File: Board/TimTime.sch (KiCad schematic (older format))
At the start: 56 parts, among them IC2 MCP73834-CNI_MF, J7 Conn_01x02, U1 STM32L433CCTx, Y1 7P-19.200MBP-T

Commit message: Initial Board Layout
Rough pass of component layout. Working down the overall footprint of the device. Also updated a couple components in the schematic.
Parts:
- removed SW? (x3): SW_Push, symbol Switch:SW_Push
- added J6: Conn_01x02, Connector_PinHeader_2.54mm:PinHeader_1x02_P2.54mm_Vertical, symbol Connector_Generic:Conn_01x02
- added S1, S2: PTS647SM70SMTR2LFS, PTS647SM70SMTR2LFS:PTS647SM38SMTR2LFS, symbol PTS647SM70SMTR2LFS:PTS647SM70SMTR2LFS
- added S3: KSS241GLFS, KSS241GLFS:KSS241GLFS, symbol KSS241GLFS:KSS241GLFS
- Brd1: renamed from Brd?; footprint (none) -> SSD1306:128x64OLED
- C13: renamed from C12; value 4.7uF -> 12uF
- D2: renamed from D?; footprint (none) -> Diode_SMD:D_SOD-123
- IC2: renamed from IC?; footprint SOT95P280X100-5N -> LT1761ES5-2:SOT95P280X100-5N
- J1: renamed from J?; footprint GCT_USB4085-GF-A_REVA -> USB4085-GF-A_REVA:GCT_USB4085-GF-A_REVA
- J2: renamed from J?; footprint CUI_SJ1-3523NG -> SJ1-3523NG:CUI_SJ1-3523NG
- J3: renamed from J?; footprint (none) -> Connector_PinHeader_2.54mm:PinHeader_1x04_P2.54mm_Vertical
- J4: renamed from J?; footprint (none) -> Connector_PinHeader_2.54mm:PinHeader_1x06_P2.54mm_Vertical
- R10, R11, R9: renamed from R?; footprint (none) -> Resistor_SMD:R_0603_1608Metric_Pad1.05x0.95mm_HandSolder
- U2: renamed from U?; footprint SOT95P280X145-5N -> 24AA00T_OT:SOT95P280X145-5N
- gave numbers to parts that had none: 8
- renumbered C13 to C12, C11 to C15, C14 to C16, C3 to C4, C4 to C5, C5 to C6, IC2 to IC1, J7 to J5, R5 to R1, R9 to R12, R10 to R13, R11 to R16, R12 to R17, R13 to R18, R6 to R2, R1 to R4, R2 to R5, R3 to R6, R4 to R8
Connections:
- net labels added: OSC
- wire segments 199 -> 228
- no-connect marks 22 -> 20
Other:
- note added: "OSC"
- moved on the sheet: J4, J5, R15, R19

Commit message: Update layout
Smaller footprint
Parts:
- added R20: 2K, Resistor_SMD:R_0603_1608Metric_Pad1.05x0.95mm_HandSolder, symbol Device:R_Small
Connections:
- net GND: now also R20.2; no longer R16.2
- new net: R16.2, R20.1
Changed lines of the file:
@@
 L power:GND #PWR043
 U 1 1 5FE4CC6E
-P 10000 3700
-F 0 "#PWR043" H 10000 3450 50  0001 C CNN
-F 1 "GND" H 10000 3550 50  0000 C CNN
-F 2 "" H 10000 3700 50  0001 C CNN
-F 3 "" H 10000 3700 50  0001 C CNN
-	1    10000 3700
+P 10000 3950
+F 0 "#PWR043" H 10000 3700 50  0001 C CNN
+F 1 "GND" H 10000 3800 50  0000 C CNN
+F 2 "" H 10000 3950 50  0001 C CNN
+F 3 "" H 10000 3950 50  0001 C CNN
+	1    10000 3950
 	1    0    0    -1
 $EndComp
@@
 Wire Wire Line
 	10900 5900 10900 6000
+$Comp
+L Device:R_Small R20
+U 1 1 60DAE3C0
+P 10000 3800
+F 0 "R20" H 10059 3846 50  0000 L CNN
+F 1 "2K" H 10059 3755 50  0000 L CNN
+F 2 "Resistor_SMD:R_0603_1608Metric_Pad1.05x0.95mm_HandSolder" H 10000 3800 50  0001 C CNN
+F 3 "~" H 10000 3800 50  0001 C CNN
+	1    10000 3800
+	1    0    0    -1
+$EndComp
+Wire Wire Line
+	10000 3900 10000 3950
 $EndSCHEMATC

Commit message: Updated routing
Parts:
- removed C2: 12uF, Capacitor_SMD:C_0603_1608Metric_Pad1.05x0.95mm_HandSolder, symbol Device:C_Small
- removed R4: 1M, Resistor_SMD:R_0603_1608Metric_Pad1.05x0.95mm_HandSolder, symbol Device:R_Small
- Brd1: symbol SSD1306-128x64_OLED:SSD1306 -> TimTime-rescue:SSD1306-SSD1306-128x64_OLED
- IC2: symbol LT1761ES5-2.8#TRMPBF:LT1761ES5-2.8#TRMPBF -> TimTime-rescue:LT1761ES5-2.8#TRMPBF-LT1761ES5-2.8#TRMPBF
- J1: symbol USB4085-GF-A_REVA:USB4085-GF-A_REVA -> TimTime-rescue:USB4085-GF-A_REVA-USB4085-GF-A_REVA
- J2: symbol SJ1-3523NG:SJ1-3523NG -> TimTime-rescue:SJ1-3523NG-SJ1-3523NG
- S1, S2: symbol PTS647SM70SMTR2LFS:PTS647SM70SMTR2LFS -> TimTime-rescue:PTS647SM70SMTR2LFS-PTS647SM70SMTR2LFS
- S3: symbol KSS241GLFS:KSS241GLFS -> TimTime-rescue:KSS241GLFS-KSS241GLFS
- U2: symbol 24AA00T_OT:24AA00T_OT -> TimTime-rescue:24AA00T_OT-24AA00T_OT
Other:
- note removed: "BOOT0 Reset"
- moved on the sheet: D1, R8
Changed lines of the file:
@@
 Text Notes 5950 1550 0    50   ~ 0
 MCU Analog Filter
-Text Notes 2400 3050 0    50   ~ 0
+Text Notes 1200 3050 0    50   ~ 0
 Status LED
 Wire Notes Line
-	1750 3100 1750 2000
-Wire Notes Line
-	2900 3100 1750 3100
-Wire Notes Line
-	2900 2000 2900 3100
-Wire Notes Line
-	1750 2000 2900 2000
-Wire Wire Line
-	2100 2750 2100 2850
+	550  3100 550  2000
+Wire Notes Line
+	1700 3100 550  3100
+Wire Notes Line
+	1700 2000 1700 3100
+Wire Notes Line
+	550  2000 1700 2000
+Wire Wire Line
+	900  2750 900  2850
 $Comp
 L power:GND #PWR011
 U 1 1 5FF4BF69
-P 2100 2850
-F 0 "#PWR011" H 2100 2600 50  0001 C CNN
-F 1 "GND" H 2105 2677 50  0000 C CNN
-F 2 "" H 2100 2850 50  0001 C CNN
-F 3 "" H 2100 2850 50  0001 C CNN
-	1    2100 2850
-	1    0    0    -1
-$EndComp
-Wire Wire Line
-	2100 2450 2100 2550
-Wire Wire Line
-	2100 2150 2100 2250
-Wire Wire Line
-	2250 2150 2100 2150
-Text GLabel 2250 2150 2    50   Input ~ 0
+P 900 2850
+F 0 "#PWR011" H 900 2600 50  0001 C CNN
+F 1 "GND" H 905 2677 50  0000 C CNN
+F 2 "" H 900 2850 50  0001 C CNN
+F 3 "" H 900 2850 50  0001 C CNN
+	1    900  2850
+	1    0    0    -1
+$EndComp
+Wire Wire Line
+	900  2450 900  2550
+Wire Wire Line
+	900  2150 900  2250
+Wire Wire Line
+	1050 2150 900  2150
+Text GLabel 1050 2150 2    50   Input ~ 0
 LED_STATUS
 $Comp
 L Device:R_Small R8
 U 1 1 5FF3E941
-P 2100 2650
-F 0 "R8" H 2159 2696 50  0000 L CNN
-F 1 "30" H 2159 2605 50  0000 L CNN
-F 2 "Resistor_SMD:R_0603_1608Metric_Pad1.05x0.95mm_HandSolder" H 2100 2650 50  0001 C CNN
-F 3 "~" H 2100 2650 50  0001 C CNN
-	1    2100 2650
+P 900 2650
+F 0 "R8" H 959 2696 50  0000 L CNN
+F 1 "30" H 959 2605 50  0000 L CNN
+F 2 "Resistor_SMD:R_0603_1608Metric_Pad1.05x0.95mm_HandSolder" H 900 2650 50  0001 C CNN
+F 3 "~" H 900 2650 50  0001 C CNN
+	1    900  2650
 	1    0    0    -1
 $EndComp
@@
 L Device:LED_Small D1
 U 1 1 5FF3CEBF
-P 2100 2350
-F 0 "D1" V 2146 2280 50  0000 R CNN
-F 1 "BLUE" V 2055 2280 50  0000 R CNN
-F 2 "LED_SMD:LED_1206_3216Metric_Pad1.42x1.75mm_HandSolder" V 2100 2350 50  0001 C CNN
-F 3 "~" V 2100 2350 50  0001 C CNN
-	1    2100 2350
+P 900 2350
+F 0 "D1" V 946 2280 50  0000 R CNN
+F 1 "BLUE" V 855 2280 50  0000 R CNN
+F 2 "LED_SMD:LED_1206_3216Metric_Pad1.42x1.75mm_HandSolder" V 900 2350 50  0001 C CNN
+F 3 "~" V 900 2350 50  0001 C CNN
+	1    900  2350
 	0    -1   -1   0
 $EndComp
-Text Notes 600  3050 0    50   ~ 0
-BOOT0 Reset
-Wire Notes Line
-	550  3100 550  2000
-Wire Notes Line
-	1650 3100 550  3100
-Wire Notes Line
-	1650 2000 1650 3100
-Wire Notes Line
-	550  2000 1650 2000
 Text Notes 600  1900 0    50   ~ 0
 TXCO
@@
 Wire Notes Line
 	3350 1950 550  1950
-Wire Wire Line
-	1250 2550 1250 2500
-Connection ~ 1250 2550
-Wire Wire Line
-	1100 2550 1250 2550
-Wire Wire Line
-	1100 2500 1100 2550
-Wire Wire Line
-	1250 2600 1250 2550
-$Comp
-L power:GND #PWR08
-U 1 1 5FE06E7D
-P 1250 2600
-F 0 "#PWR08" H 1250 2350 50  0001 C CNN
-F 1 "GND" H 1255 2427 50  0000 C CNN
-F 2 "" H 1250 2600 50  0001 C CNN
-F 3 "" H 1250 2600 50  0001 C CNN
-	1    1250 2600
-	1    0    0    -1
-$EndComp
-Wire Wire Line
-	1250 2250 1250 2300
-Connection ~ 1250 2250
-Wire Wire Line
-	1100 2250 1250 2250
-Wire Wire Line
-	1100 2300 1100 2250
-Wire Wire Line
-	1250 2150 1250 2250
-Wire Wire Line
-	1150 2150 1250 2150
-$Comp
-L Device:C_Small C2
-U 1 1 5FE049E6
-P 1250 2400
-F 0 "C2" H 1342 2446 50  0000 L CNN
-F 1 "12uF" H 1342 2355 50  0000 L CNN
-F 2 "Capacitor_SMD:C_0603_1608Metric_Pad1.05x0.95mm_HandSolder" H 1250 2400 50  0001 C CNN
-F 3 "~" H 1250 2400 50  0001 C CNN
-	1    1250 2400
-	1    0    0    -1
-$EndComp
-Text GLabel 1150 2150 0    50   Input ~ 0
-BOOT0
-$Comp
-L Device:R_Small R4
-U 1 1 5FDB4DA9
-P 1100 2400
-F 0 "R4" V 904 2400 50  0000 C CNN
-F 1 "1M" V 995 2400 50  0000 C CNN
-F 2 "Resistor_SMD:R_0603_1608Metric_Pad1.05x0.95mm_HandSolder" H 1100 2400 50  0001 C CNN
-F 3 "~" H 1100 2400 50  0001 C CNN
-	1    1100 2400
-	1    0    0    -1
-$EndComp
-$Comp
-L LT1761ES5-2.8#TRMPBF:LT1761ES5-2.8#TRMPBF IC2
+$Comp
+L TimTime-rescue:LT1761ES5-2.8#TRMPBF-LT1761ES5-2.8#TRMPBF IC2
 U 1 1 609D162F
 P 8800 1150
@@
 	550  3150 1650 3150
 $Comp
-L USB4085-GF-A_REVA:USB4085-GF-A_REVA J1
+L TimTime-rescue:USB4085-GF-A_REVA-USB4085-GF-A_REVA J1
 U 1 1 60EA7903
 P 1300 5600
@@
 	1900 7750 550  7750
 $Comp
-L SJ1-3523NG:SJ1-3523NG J2
+L TimTime-rescue:SJ1-3523NG-SJ1-3523NG J2
 U 1 1 608E50D0
 P 2500 7300
@@
 NoConn ~ 3100 7300
 $Comp
-L 24AA00T_OT:24AA00T_OT U2
+L TimTime-rescue:24AA00T_OT-24AA00T_OT U2
 U 1 1 609233E5
 P 7100 5850
@@
 TC Input/Output
 $Comp
-L SSD1306-128x64_OLED:SSD1306 Brd1
+L TimTime-rescue:SSD1306-SSD1306-128x64_OLED Brd1
 U 1 1 60FA55A1
 P 2500 5100
@@
 	1000 950  1450 950
 $Comp
-L PTS647SM70SMTR2LFS:PTS647SM70SMTR2LFS S1
+L TimTime-rescue:PTS647SM70SMTR2LFS-PTS647SM70SMTR2LFS S1
 U 1 1 609708D6
 P 8500 6300
@@
 Connection ~ 8350 5850
 $Comp
-L PTS647SM70SMTR2LFS:PTS647SM70SMTR2LFS S2
+L TimTime-rescue:PTS647SM70SMTR2LFS-PTS647SM70SMTR2LFS S2
 U 1 1 60A438F2
 P 9500 6300
@@
 Connection ~ 9750 5900
 $Comp
-L KSS241GLFS:KSS241GLFS S3
+L TimTime-rescue:KSS241GLFS-KSS241GLFS S3
 U 1 1 60B48A83
 P 10600 5700

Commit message: V02 routing. VddUSB
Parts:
- added C17, C2: 1.2uF, Capacitor_SMD:C_0603_1608Metric_Pad1.08x0.95mm_HandSolder, symbol Device:C_Small
- added C18: 100nF, Capacitor_SMD:C_0603_1608Metric_Pad1.08x0.95mm_HandSolder, symbol Device:C_Small
- added IC3: LTC1844ES5-3.3#TRPBF, LT1761ES5-2.8#TRMPBF:SOT95P280X100-5N, symbol TimTime-rescue:LT1761ES5-2.8#TRMPBF-LT1761ES5-2.8#TRMPBF
- IC2: footprint LT1761ES5-2:SOT95P280X100-5N -> LT1761ES5-2.8#TRMPBF:SOT95P280X100-5N
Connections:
- net +2V8: no longer C5.1, U1.36 (VDDUSB)
- net +BATT: now also C2.1, IC3.1 (IN), IC3.3 (~SHDN)
- net BTN_PWR: now also U1.10 (PA0); no longer U1.18 (PB0)
- net GND: now also C17.2, C18.1, C2.2, IC3.2 (GND)
- net BOOT0: no longer names the net of U1.44 (PH3)
- new net: C18.2, IC3.4 (BYP)
- new net +3V3: C17.1, C5.1, IC3.5 (OUT), U1.36 (VDDUSB)
- no-connect marks 20 -> 21
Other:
- note added: "3.3V LDO Regulator"
- moved on the sheet: C5, C6, C7, C8

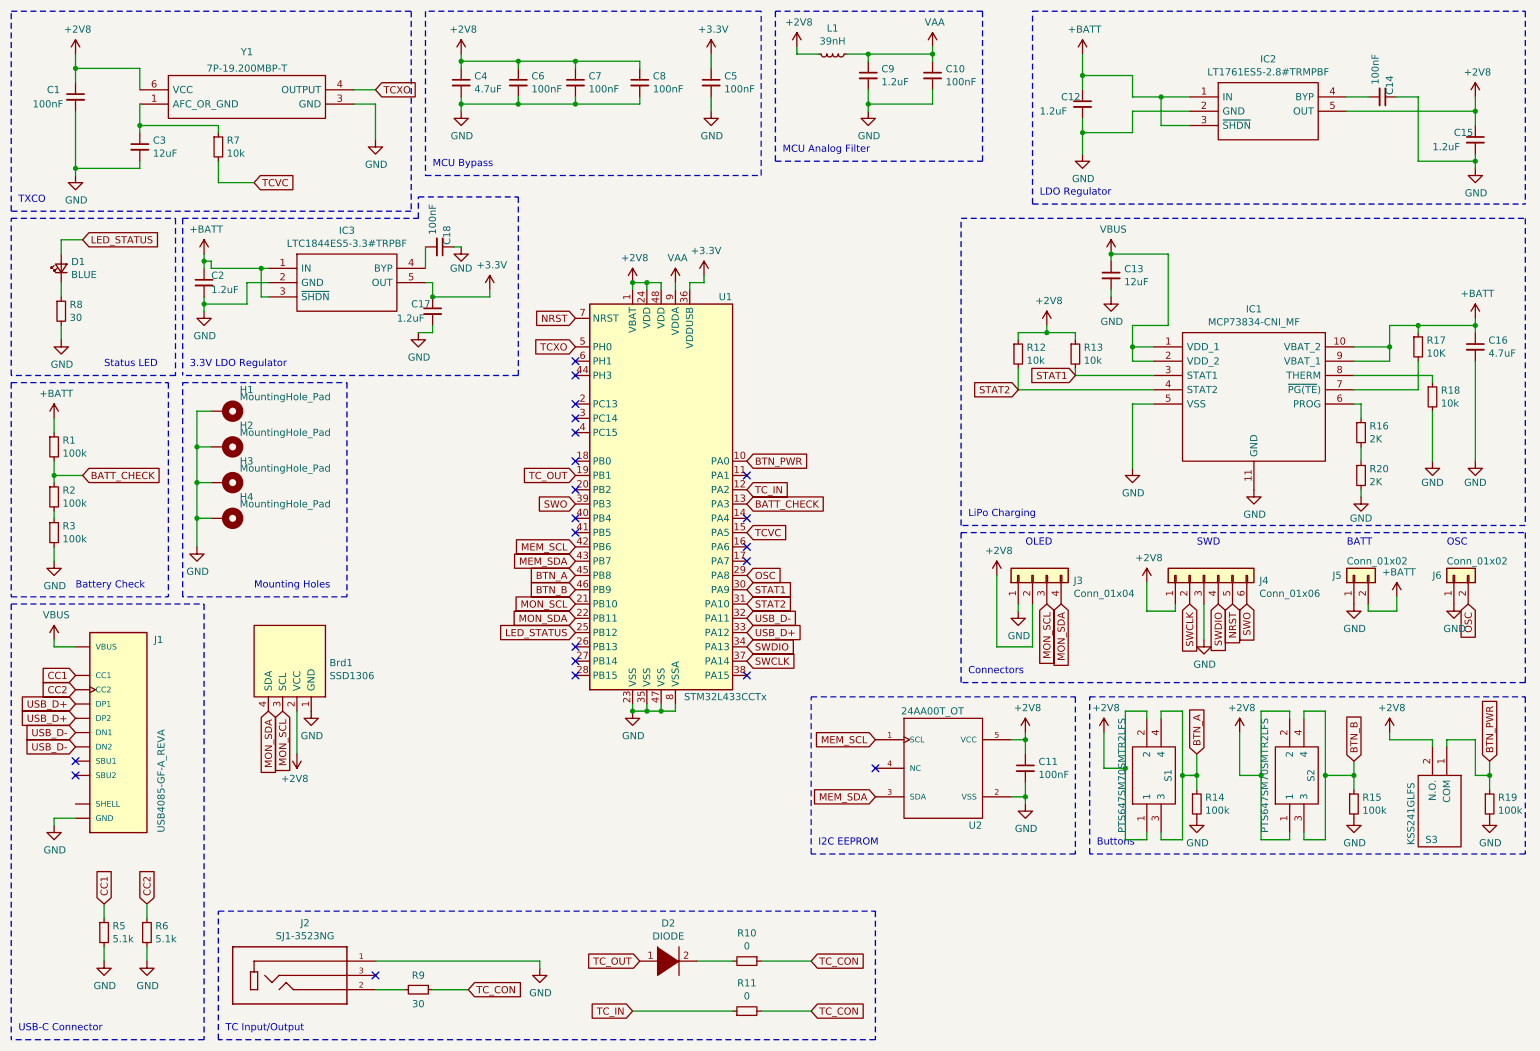
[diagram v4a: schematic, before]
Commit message: Add additional button, include libraries
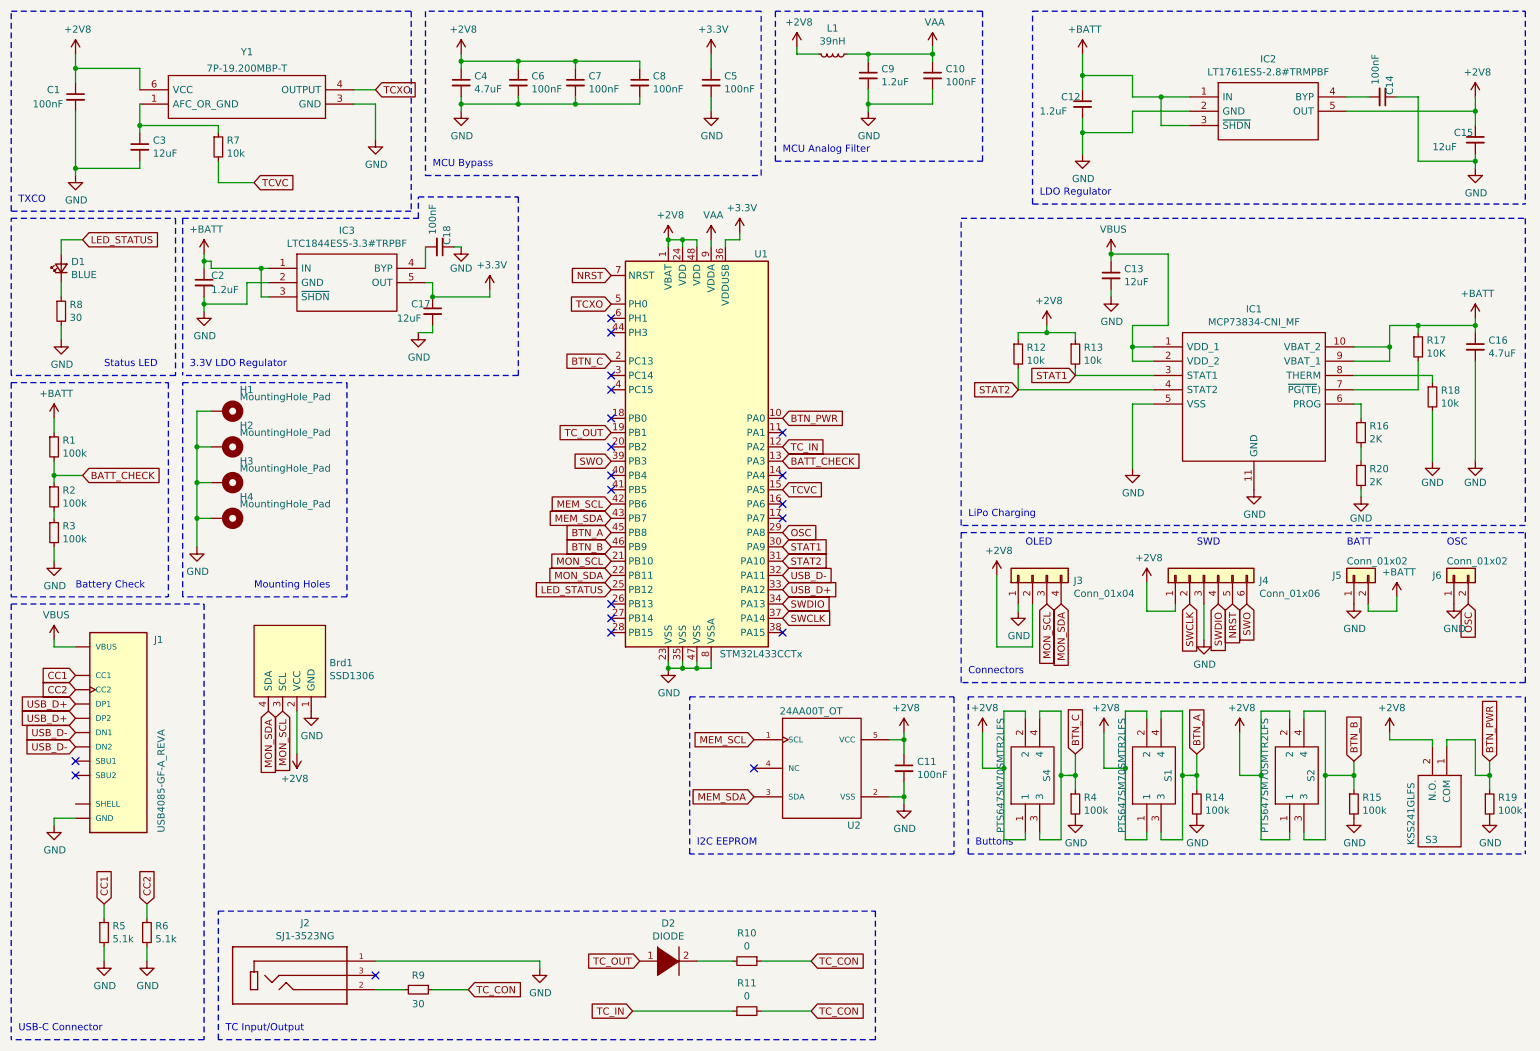
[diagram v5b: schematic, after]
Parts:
- added R4: 100k, Resistor_SMD:R_0603_1608Metric_Pad1.05x0.95mm_HandSolder, symbol Device:R_Small
- added S4: PTS647SM70SMTR2LFS, PTS647SM70SMTR2LFS:PTS647SM38SMTR2LFS, symbol TimTime-rescue:PTS647SM70SMTR2LFS-PTS647SM70SMTR2LFS
- C15, C17: value 1.2uF -> 12uF
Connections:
- net +2V8: now also S4.1, S4.2
- net GND: now also R4.2
- net BTN_C: now reaches U1.2 (PC13)
- net BTN_C: now also R4.1, S4.3, S4.4
- no-connect marks 21 -> 20
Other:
- moved on the sheet: C11, U1, U2

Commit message: V01 Gerbers
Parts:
- H1, H2, H3, H4: footprint MountingHole:MountingHole_2.7mm_M2.5_Pad_Via -> MountingHole:MountingHole_3.2mm_M3_Pad_Via
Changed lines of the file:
@@
 F 0 "H4" V 1900 4200 50  0000 L CNN
 F 1 "MountingHole_Pad" V 1950 4200 50  0000 L CNN
-F 2 "MountingHole:MountingHole_2.7mm_M2.5_Pad_Via" H 2050 4100 50  0001 C CNN
+F 2 "MountingHole:MountingHole_3.2mm_M3_Pad_Via" H 2050 4100 50  0001 C CNN
 F 3 "~" H 2050 4100 50  0001 C CNN
 	1    2050 4100
@@
 F 0 "H3" V 1900 3950 50  0000 L CNN
 F 1 "MountingHole_Pad" V 1950 3950 50  0000 L CNN
-F 2 "MountingHole:MountingHole_2.7mm_M2.5_Pad_Via" H 2050 3850 50  0001 C CNN
+F 2 "MountingHole:MountingHole_3.2mm_M3_Pad_Via" H 2050 3850 50  0001 C CNN
 F 3 "~" H 2050 3850 50  0001 C CNN
 	1    2050 3850
@@
 F 0 "H2" V 1900 3700 50  0000 L CNN
 F 1 "MountingHole_Pad" V 1950 3700 50  0000 L CNN
-F 2 "MountingHole:MountingHole_2.7mm_M2.5_Pad_Via" H 2050 3600 50  0001 C CNN
+F 2 "MountingHole:MountingHole_3.2mm_M3_Pad_Via" H 2050 3600 50  0001 C CNN
 F 3 "~" H 2050 3600 50  0001 C CNN
 	1    2050 3600
@@
 F 0 "H1" V 1900 3450 50  0000 L CNN
 F 1 "MountingHole_Pad" V 1950 3450 50  0000 L CNN
-F 2 "MountingHole:MountingHole_2.7mm_M2.5_Pad_Via" H 2050 3350 50  0001 C CNN
+F 2 "MountingHole:MountingHole_3.2mm_M3_Pad_Via" H 2050 3350 50  0001 C CNN
 F 3 "~" H 2050 3350 50  0001 C CNN
 	1    2050 3350
